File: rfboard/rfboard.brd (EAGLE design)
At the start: 30 x 60 mm, 17 parts, among them U1 MAX1555

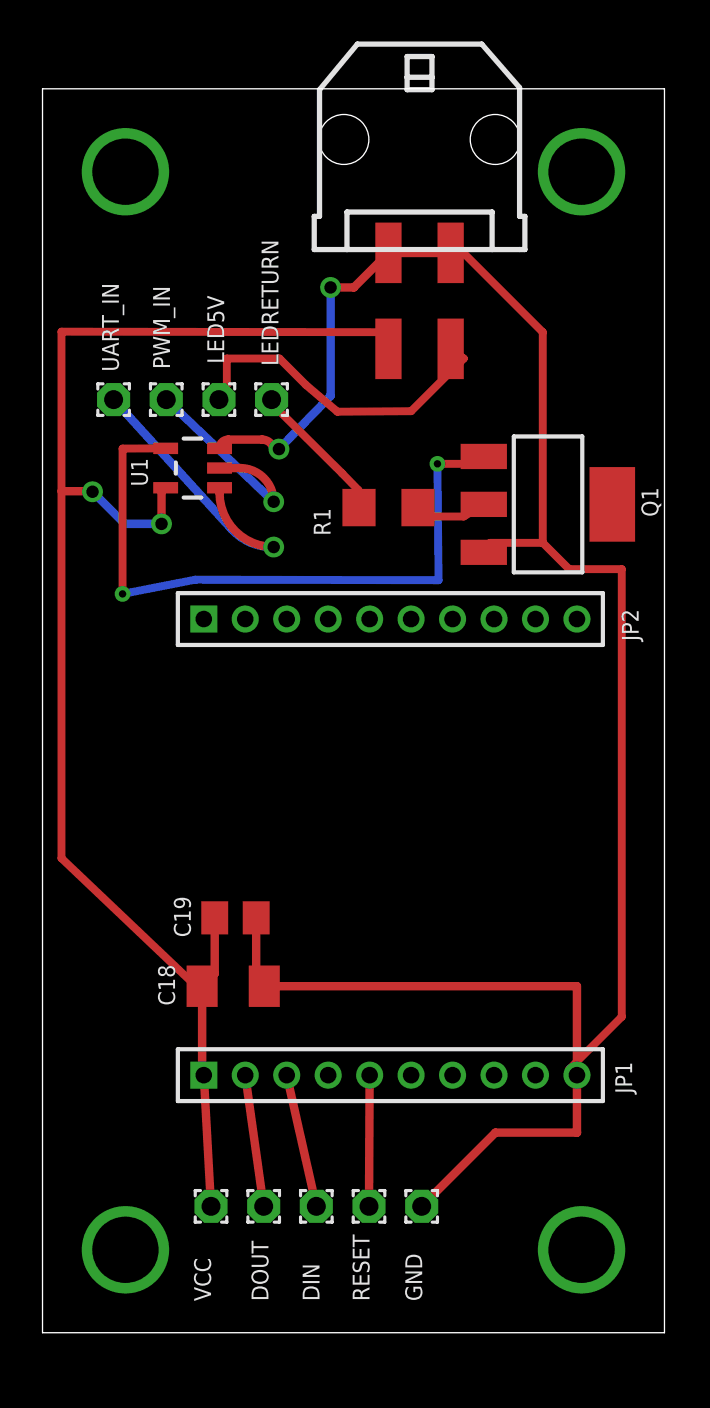
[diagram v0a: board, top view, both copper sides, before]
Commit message: changing the RF board to include voltage dividers
- rearranged board to include pin headers
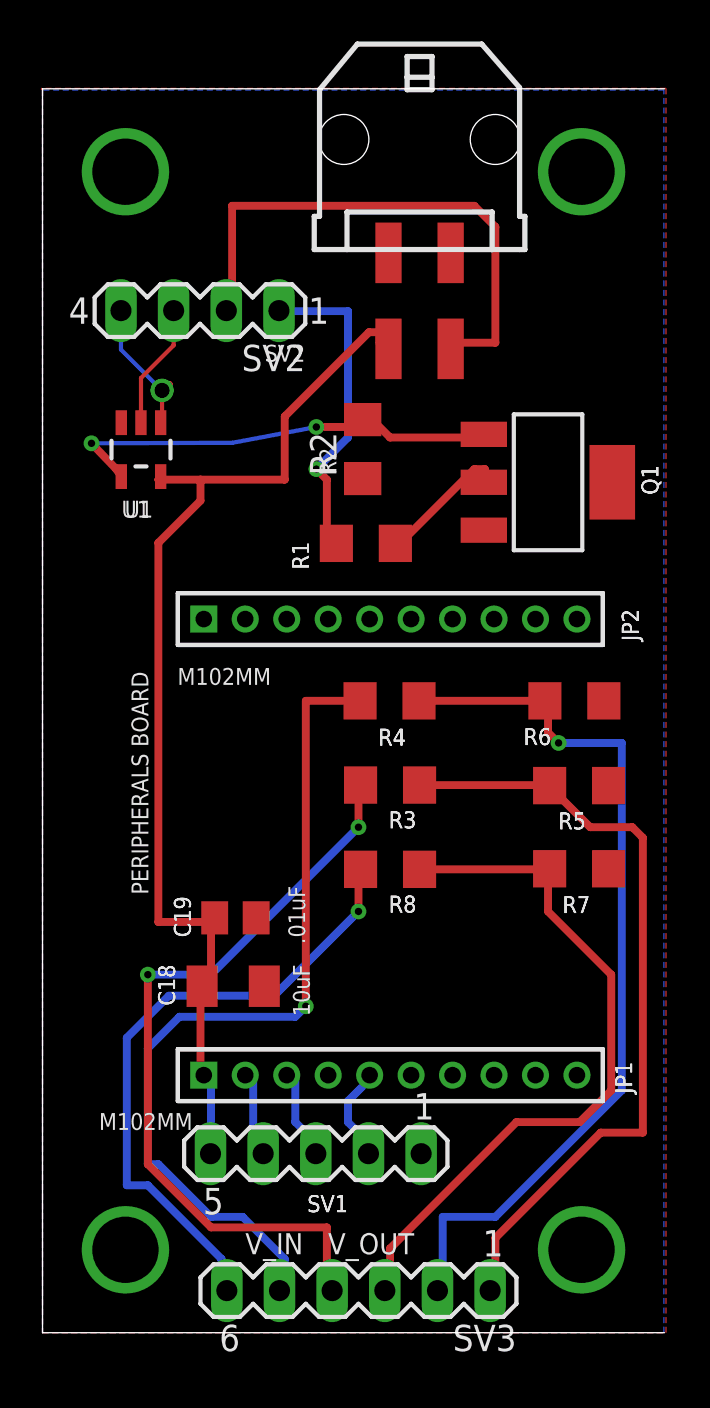
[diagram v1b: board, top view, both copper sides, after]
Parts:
- removed DIN, DOUT, GND, LED5V, LEDRETURN, PWM_IN, RESET, UART_IN, VCC: (no value), wirepad:1,6/0,9
- added R2, R3, R4, R5, R6, R7, R8: (no value), rcl:R1206
- added SV1: (no value), con-lstb:MA05-1
- added SV2: (no value), con-lstb:MA04-1
- added SV3: (no value), con-lstb:MA06-1
- moved U1 2.64 mm to (4.75, 42.6), turned to 180 degrees
- moved R1 2.04 mm to (15.6, 38.1)
- moved Q1 1.07 mm to (24.4, 41.0)
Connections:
- removed net 3.3V-2: C18.1, C19.1, JP1.1, U1.5, VCC.1, X2.P$3
- removed net GND2: C18.2, C19.2, GND.1, JP1.10, Q1.3, U1.3, X2.P$1, X2.P$2
- removed net N$1: DOUT.1, JP1.2
- removed net N$2: DIN.1, JP1.3
- removed net N$4: JP1.5, RESET.1
- removed net N$6: U1.1, UART_IN.1
- removed net N$7: PWM_IN.1, U1.2
- removed net N$8: LEDRETURN.1, R1.2
- removed net N$9: LED5V.1, X2.P$4
- new net DIN: JP1.3, SV1.3
- new net DOUT: JP1.2, SV1.4
- new net GND: C18.2, C19.2, JP1.10, Q1.3, R2.1, R5.1, R6.1, R7.1, SV1.1, U1.3, X2.P$1, X2.P$2
- new net LED5V: SV2.2, X2.P$4
- new net LEDRETURN: R1.2, SV2.1
- new net PWM_IN: SV2.3, U1.2
- new net RESET: JP1.5, SV1.2
- new net UART_IN: SV2.4, U1.1
- new net VCC: C18.1, C19.1, JP1.1, SV1.5, U1.5, X2.P$3
- new net VD1: R3.1, R5.2, SV3.1
- new net VD2: R4.1, R6.2, SV3.2
- new net VD3: R7.2, R8.1, SV3.3
- new net V_1: R3.2, SV3.4
- new net V_2: R4.2, SV3.5
- new net V_3: R8.2, SV3.6
- net N$3: now also R2.2
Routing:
- net GND2: track 103.4 -> 0.00 mm, vias 2 -> 0
- net 3.3V-2: track 72.8 -> 0.00 mm, vias 2 -> 0
- net VCC: track 0.00 -> 53.4 mm
- net VD2: track 0.00 -> 43.2 mm, vias 0 -> 1
- net V_2: track 0.00 -> 41.7 mm, vias 0 -> 1
- net VD1: track 0.00 -> 38.1 mm
- net V_1: track 0.00 -> 37.6 mm, vias 0 -> 2
- net VD3: track 0.00 -> 34.3 mm
- net V_3: track 0.00 -> 30.8 mm, vias 0 -> 1
- net LED5V: track 0.00 -> 26.2 mm
- net N$9: track 16.3 -> 0.00 mm
- net LEDRETURN: track 0.00 -> 15.8 mm, vias 0 -> 1
- net N$6: track 14.6 -> 0.00 mm, vias 1 -> 0
- net N$3: track 32.3 -> 21.8 mm
- net N$7: track 10.4 -> 0.00 mm, vias 1 -> 0
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- added copper zone on layer 1, net GND
- added copper zone on layer 16, net GND
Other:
- board text added: ".01uF"
- board text added: "10uF"
- board text added: "C18"
- board text added: "C19"
- board text added: "JP1"
- board text added: "JP2"
- board text added: "M102MM"
- board text added: "Q1"
- board text added: "R1"
- board text added: "R2"
- board text added: "R3"
- board text added: "R4"
- board text added: "R5"
- board text added: "R6"
- board text added: "R7"
- board text added: "R8"
- board text added: "SV1"
- board text added: "SV2"
- board text added: "U1"
- board text added: "V_IN V_OUT"

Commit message: changed headers and finished board
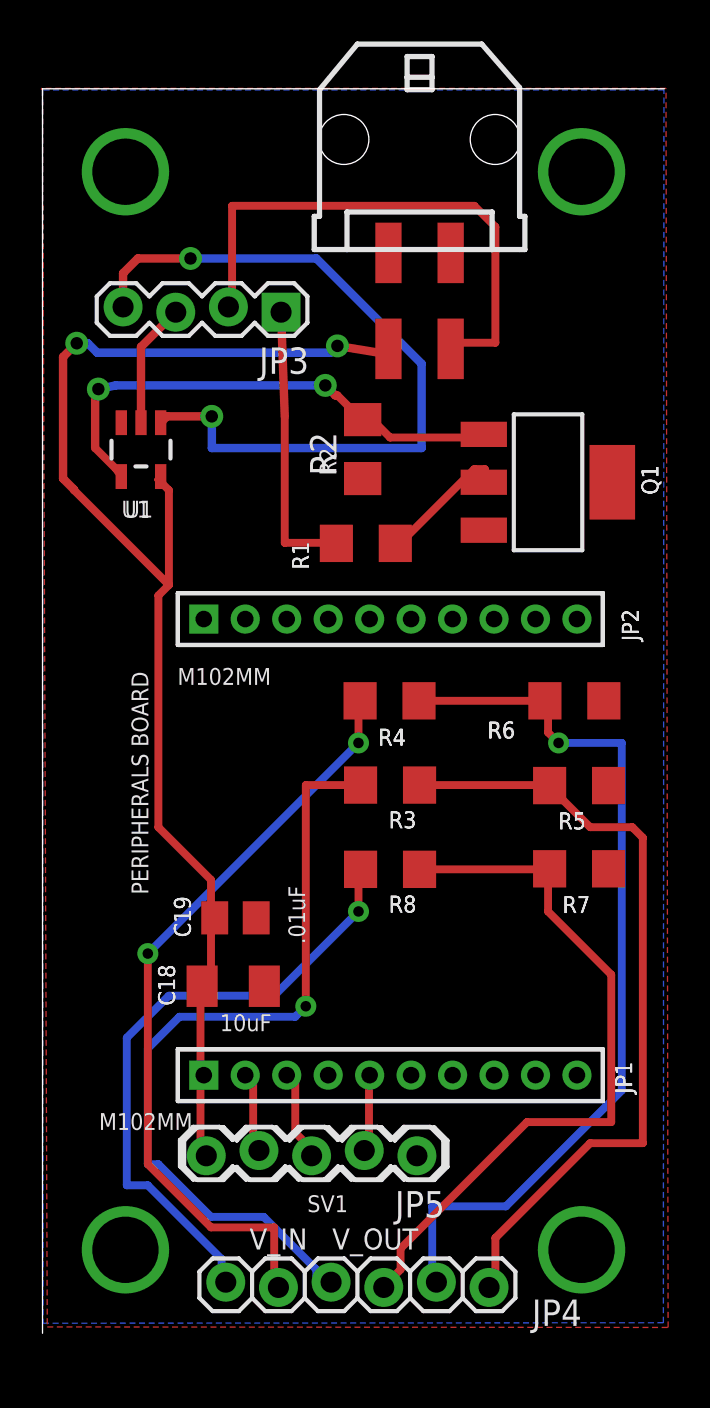
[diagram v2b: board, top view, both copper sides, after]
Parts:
- removed SV1: (no value), con-lstb:MA05-1
- removed SV2: (no value), con-lstb:MA04-1
- removed SV3: (no value), con-lstb:MA06-1
- added JP3: (no value), SparkFun-Connectors:1X04_LOCK
- added JP4: (no value), SparkFun-Connectors:1X06_LOCK
- added JP5: (no value), SparkFun-Connectors:1X05_LOCK
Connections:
- net DIN: now also JP5.3; no longer SV1.3
- net DOUT: now also JP5.4; no longer SV1.4
- net GND: now also JP5.1; no longer SV1.1
- net LED5V: now also JP3.2; no longer SV2.2
- net LEDRETURN: now also JP3.1; no longer SV2.1
- net PWM_IN: now also JP3.3; no longer SV2.3
- net RESET: now also JP5.2; no longer SV1.2
- net UART_IN: now also JP3.4; no longer SV2.4
- net VCC: now also JP5.5; no longer SV1.5
- net VD1: now also JP4.1; no longer SV3.1
- net VD2: now also JP4.2; no longer SV3.2
- net VD3: now also JP4.3; no longer SV3.3
- net V_1: now also JP4.4; no longer SV3.4
- net V_2: now also JP4.5; no longer SV3.5
- net V_3: now also JP4.6; no longer SV3.6
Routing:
- net UART_IN: track 7.10 -> 36.7 mm
- net VCC: track 53.4 -> 64.7 mm, vias 0 -> 2
- net V_2: track 41.7 -> 36.9 mm, vias 1 -> 2
- net N$3: track 21.8 -> 24.5 mm
- net LEDRETURN: track 15.8 -> 13.6 mm, vias 1 -> 0
- net V_1: track 37.6 -> 38.8 mm, vias 2 -> 1
- net RESET: track 4.90 -> 3.70 mm
- net DOUT: track 4.49 -> 3.95 mm
- net V_3: track 30.8 -> 30.2 mm
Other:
- outline, holes or cut-outs redrawn
- board text removed: "SV2"

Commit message: Changes to layout and silk screen, new gerber files
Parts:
- removed R1, R2, R3, R6, R7, R8: (no value), rcl:R1206
- added R1A, R1B, R2A, R2B, R3A, R3B: (no value), rcl:R1206
- moved R5 15.6 mm to (15.6, 38.1)
- moved R4 12.2 mm to (15.4, 42.6), turned to 90 degrees
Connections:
- net GND: now also R1B.1, R2B.1, R3B.1, R4.1; no longer R2.1, R5.1, R6.1, R7.1
- net LEDRETURN: now also R5.2; no longer R1.2
- net N$3: now also R4.2; no longer R2.2
- net N$5: now also R5.1; no longer R1.1
- net VD1: now also R1A.1, R1B.2; no longer R3.1, R5.2
- net VD2: now also R2A.1, R2B.2; no longer R4.1, R6.2
- net VD3: now also R3A.1, R3B.2; no longer R7.2, R8.1
- net V_1: now also R1A.2; no longer R3.2
- net V_2: now also R2A.2; no longer R4.2
- net V_3: now also R3A.2; no longer R8.2
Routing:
- net VD2: track 43.5 -> 33.8 mm, vias 1 -> 0
- net V_2: track 36.9 -> 31.5 mm, vias 2 -> 1
- net V_1: track 38.8 -> 43.4 mm
- net V_3: track 30.2 -> 26.8 mm
- net VD3: track 34.6 -> 31.6 mm
- net VD1: track 38.1 -> 38.8 mm
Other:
- outline, holes or cut-outs redrawn
- board text added: "A R1 B"
- board text added: "A R2 B"
- board text added: "A R3 B"
- board text removed: "R3"
- board text removed: "R4"
- board text removed: "R5"
- board text removed: "R6"
- board text removed: "R7"
- board text removed: "R8"
